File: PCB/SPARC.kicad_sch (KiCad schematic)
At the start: 86 parts, among them J1 Conn_Coaxial_Power, J2 Conn_Coaxial_Power, J3 Conn_01x06_Female, J4 Conn_01x03_Female, J5 Conn_01x03_Female, J6 Conn_01x06_Female, U1 HV2621, U2 HV2621

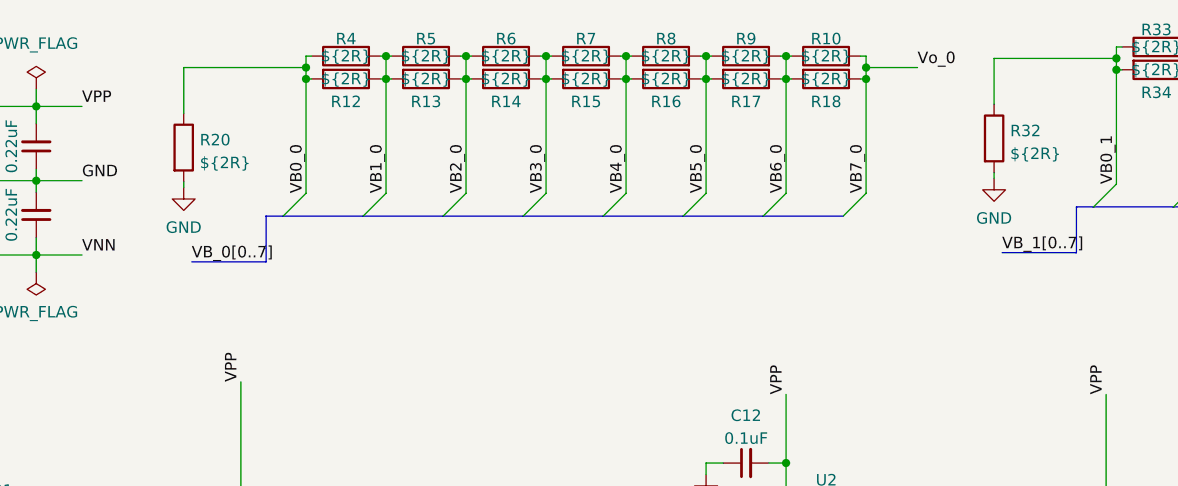
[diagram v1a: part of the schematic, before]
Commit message: Updated R20 & R32 routing
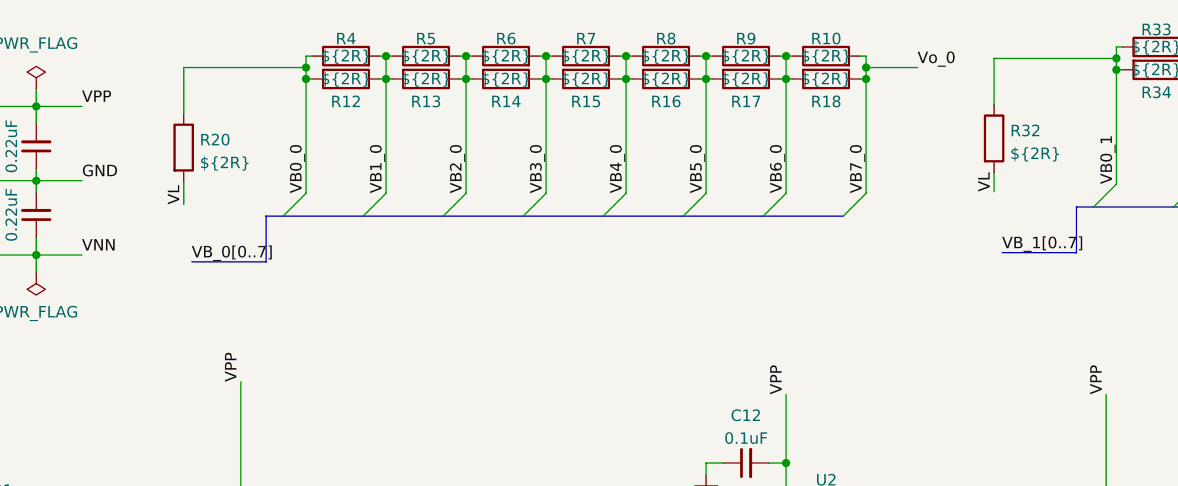
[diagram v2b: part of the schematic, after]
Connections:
- net GND: no longer R20.2, R32.2
- net VL: now also R20.2, R32.2
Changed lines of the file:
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@@
     (stroke (width 0) (type default) (color 0 0 0 0))
   )
-  (wire (pts (xy 90.678 36.322) (xy 90.678 35.687))
+  (wire (pts (xy 90.678 35.687) (xy 90.678 38.2016))
     (stroke (width 0) (type default) (color 0 0 0 0))
   )
@@
     (stroke (width 0) (type default) (color 0 0 0 0))
   )
-  (wire (pts (xy 180.721 35.306) (xy 180.721 34.671))
+  (wire (pts (xy 180.721 34.671) (xy 180.721 36.7792))
     (stroke (width 0) (type default) (color 0 0 0 0))
   )
@@
   )
   (label "CLK_1" (at 141.478 196.342 0)
+    (effects (font (size 1.27 1.27)) (justify left bottom))
+  )
+  (label "VL" (at 180.721 36.7792 90)
     (effects (font (size 1.27 1.27)) (justify left bottom))
   )
@@
   )
   (label "VB1_0" (at 113.157 36.957 90)
+    (effects (font (size 1.27 1.27)) (justify left bottom))
+  )
+  (label "VL" (at 90.678 38.2016 90)
     (effects (font (size 1.27 1.27)) (justify left bottom))
   )
@@
     (pin "9")
   )
-  (symbol (lib_id "power:GND") (at 180.721 35.306 0) (unit 1)
-    (in_bom yes) (on_board yes) (fields_autoplaced)
-    (property "Reference" "#PWR0101" (id 0) (at 180.721 41.656 0)
-      (effects (font (size 1.27 1.27)) hide)
-    )
-    (property "Value" "GND" (id 1) (at 180.721 39.7494 0))
-    (property "Footprint" "" (id 2) (at 180.721 35.306 0)
-      (effects (font (size 1.27 1.27)) hide)
-    )
-    (property "Datasheet" "" (id 3) (at 180.721 35.306 0)
-      (effects (font (size 1.27 1.27)) hide)
-    )
-    (pin "1")
-  )
   (symbol (lib_id "Device:R") (at 87.503 78.232 90) (unit 1)
     (in_bom yes) (on_board yes)
@@
     (pin "2")
   )
-  (symbol (lib_id "power:GND") (at 90.678 36.322 0) (unit 1)
-    (in_bom yes) (on_board yes) (fields_autoplaced)
-    (property "Reference" "#PWR03" (id 0) (at 90.678 42.672 0)
-      (effects (font (size 1.27 1.27)) hide)
-    )
-    (property "Value" "GND" (id 1) (at 90.678 40.7654 0))
-    (property "Footprint" "" (id 2) (at 90.678 36.322 0)
-      (effects (font (size 1.27 1.27)) hide)
-    )
-    (property "Datasheet" "" (id 3) (at 90.678 36.322 0)
-      (effects (font (size 1.27 1.27)) hide)
-    )
-    (pin "1")
-  )
   (symbol (lib_id "Device:R") (at 183.642 99.949 90) (unit 1)
     (in_bom yes) (on_board yes)
@@
       (reference "#PWR02") (unit 1) (value "GND") (footprint "")
     )
-    (path "/ad05441e-2b44-4c5e-9f86-168ee1a99750"
-      (reference "#PWR03") (unit 1) (value "GND") (footprint "")
-    )
     (path "/4f95875f-9d6a-4ae9-b0b9-0fa8ce15c56c"
       (reference "#PWR04") (unit 1) (value "GND") (footprint "")
@@
       (reference "#PWR06") (unit 1) (value "GND") (footprint "")
     )
-    (path "/29313a4a-7b41-4590-b4ba-c170ef1af02d"
-      (reference "#PWR0101") (unit 1) (value "GND") (footprint "")
-    )
     (path "/c56bbac1-2c11-455f-bab0-1a272711ddc8"

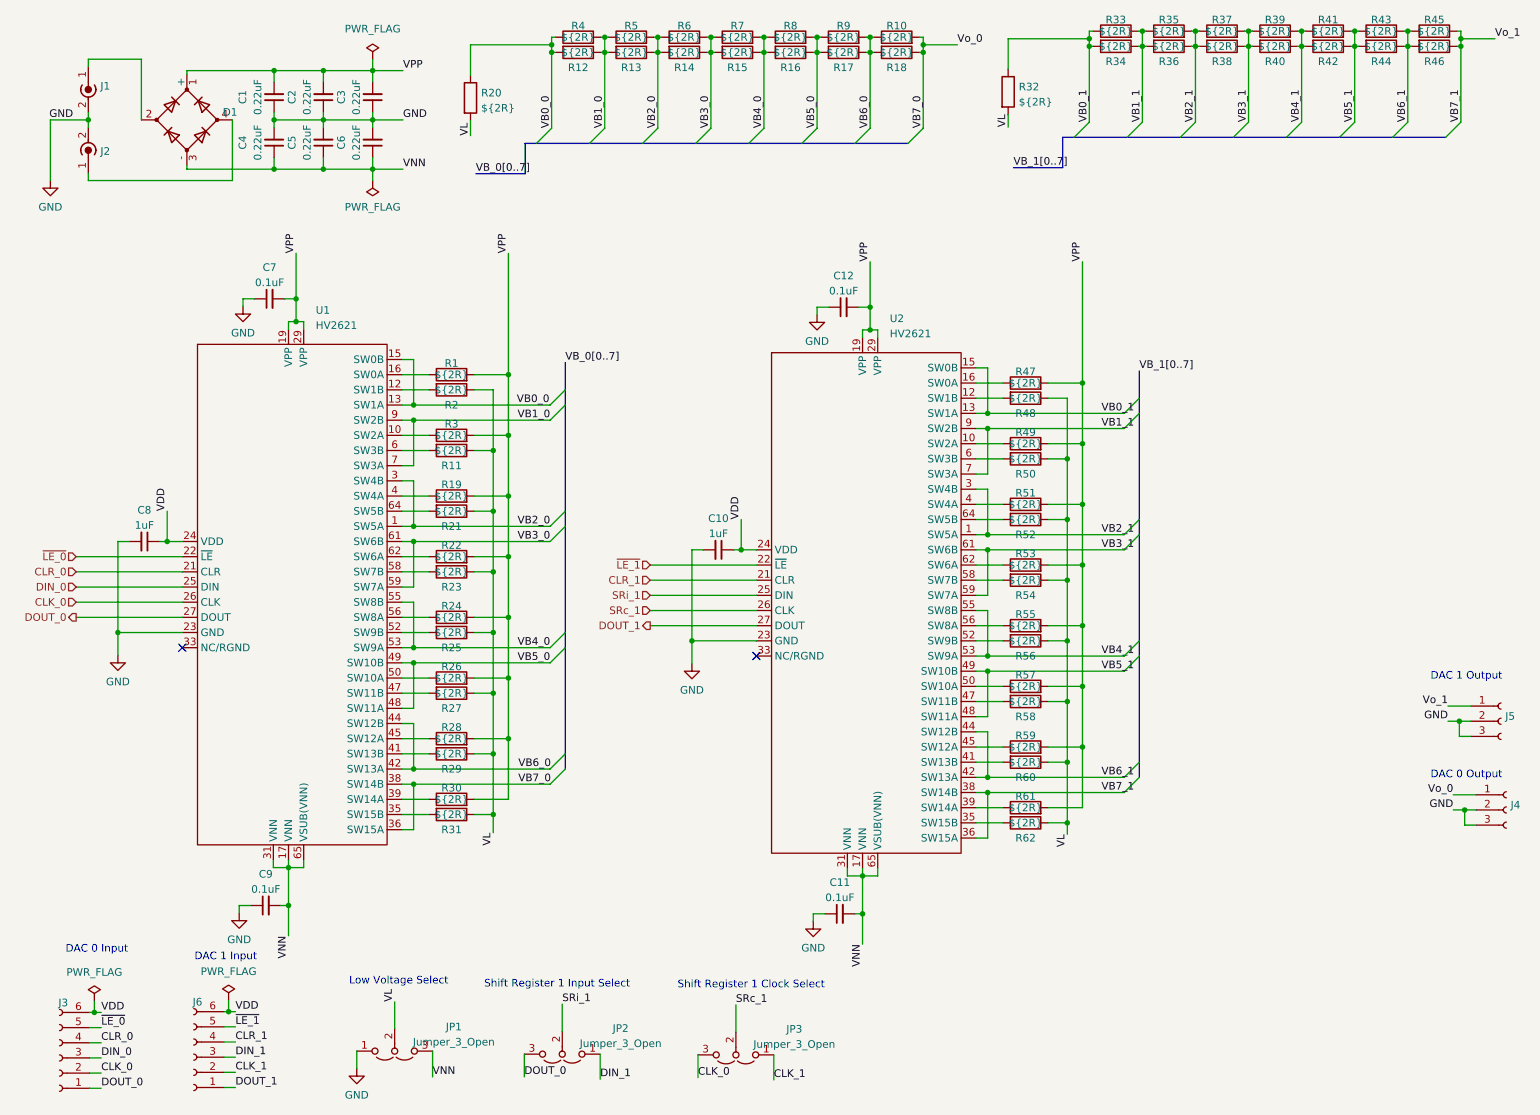
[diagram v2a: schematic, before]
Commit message: Reworked mode select jumpers
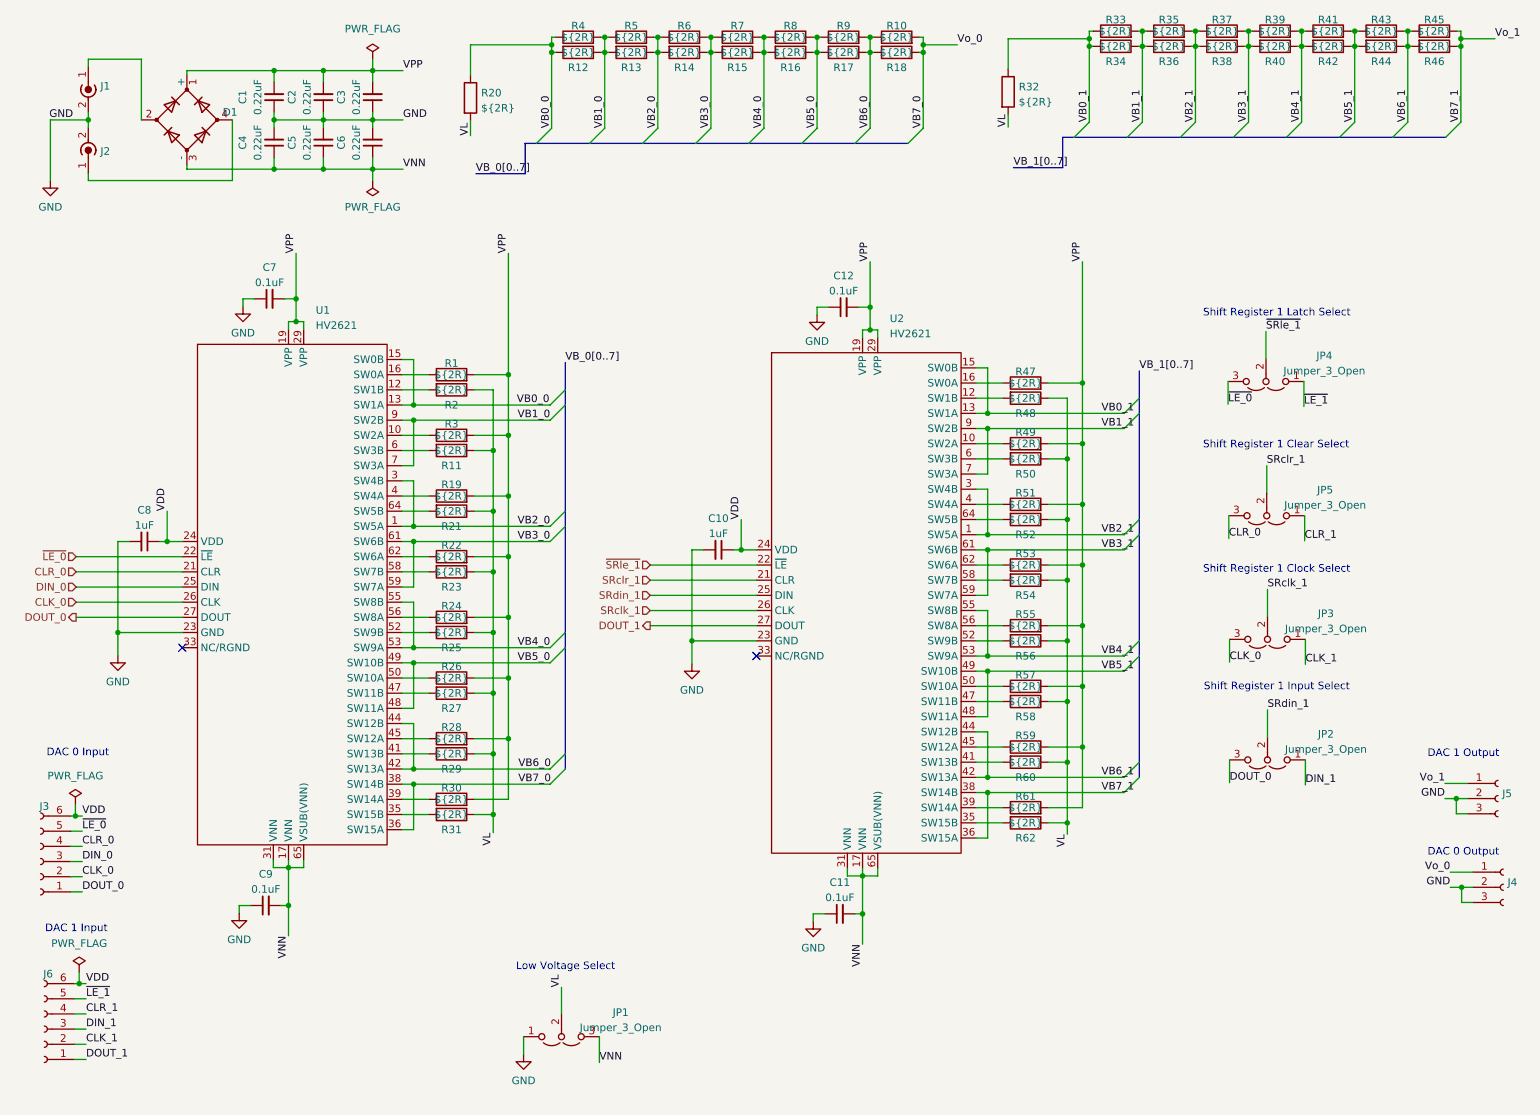
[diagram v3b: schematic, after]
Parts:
- added JP4, JP5: Jumper_3_Open, Connector_PinHeader_2.54mm:PinHeader_1x03_P2.54mm_Vertical, symbol Jumper:Jumper_3_Open
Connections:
- net CLR_0: now also JP5.3 (B)
- net CLR_1: now also JP5.1 (A); no longer U2.21 (CLR)
- net ~{LE_0}: now also JP4.3 (B)
- net ~{LE_1}: now also JP4.1 (A); no longer U2.22 (~{LE})
- net SRc_1 renamed SRclk_1
- net SRi_1 renamed SRdin_1
- new net SRclr_1: JP5.2 (C), U2.21 (CLR)
- new net ~{SRle_1}: JP4.2 (C), U2.22 (~{LE})
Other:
- note added: "Shift Register 1 Clear Select"
- note added: "Shift Register 1 Latch Select"
- moved on the sheet: J3, J4, J5, J6, JP1, JP2, JP3
